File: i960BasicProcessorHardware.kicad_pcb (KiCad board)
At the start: 4 copper layers, 169.9 x 169.8 mm, 70 parts, among them J1 Conn_02x16_Odd_Even, J10 Conn_01x03, J11 Conn_01x08, J2 Conn_02x39_Odd_Even, J3 Conn_01x03, J4 Conn_02x05_Odd_Even, J5 Conn_02x05_Odd_Even, J6 Conn_02x05_Odd_Even, J7 Conn_01x06, J8 Conn_01x06, J9 Conn_01x11, SW1 SW_Push, U1 74HC245, U10 74LS08, U11 74LS04, U12 74LS174, U13 SN74LVC245AN, U14 74LS174, U15 MCP23S17_SP, U16 MCP23S17_SP, U17 MCP23S17_SP, U18 ATtiny85-20PU, U2 80960Sx, U3 MCP23S17_SP, U4 74HC245, U5 74HC573, U6 74HC573, U7 Adafruit_FeatherWing (PSRAM F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, U8 Adafruit_FeatherWing (PSRAM F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, U9 74LS125

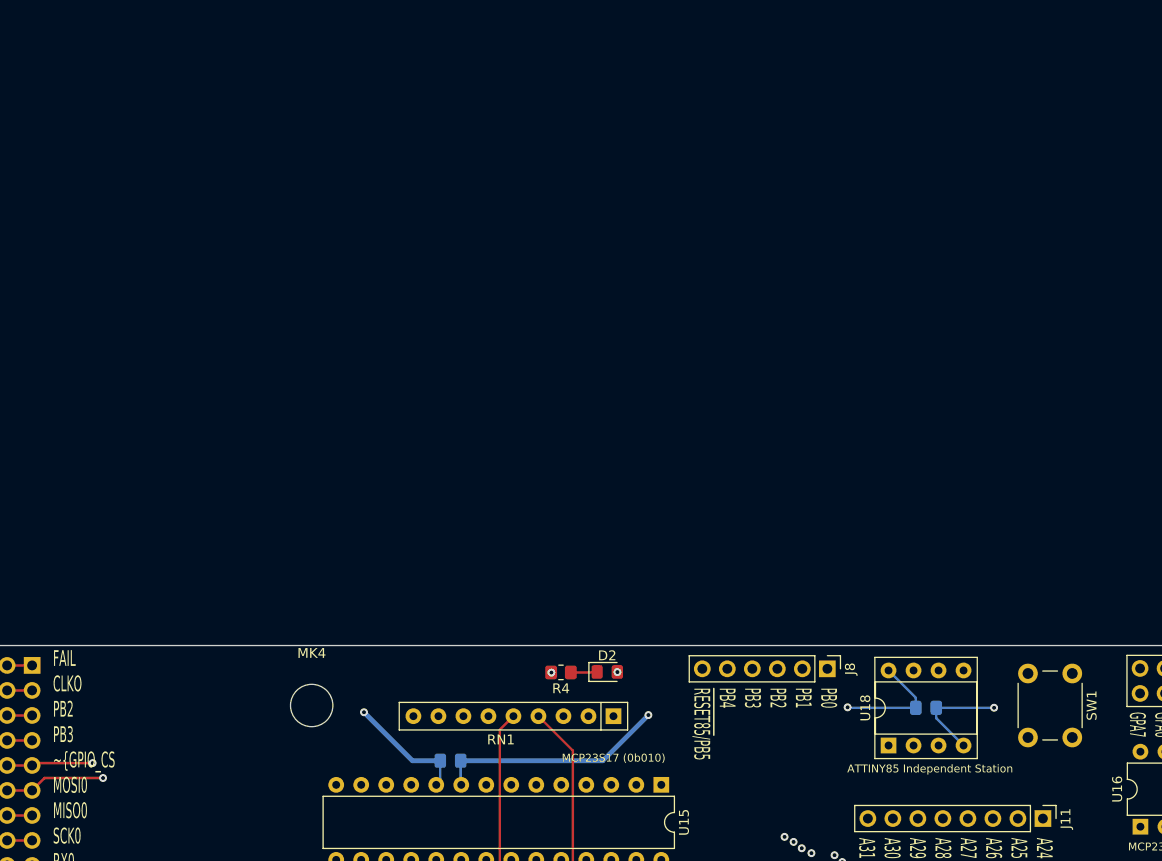
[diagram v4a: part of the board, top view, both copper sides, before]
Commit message: Drop the attiny85
I am going to place two 861s instead tied to the same 20mhz clock

I am also considering adding a dip40 socket also tied to the same
20mhz clock
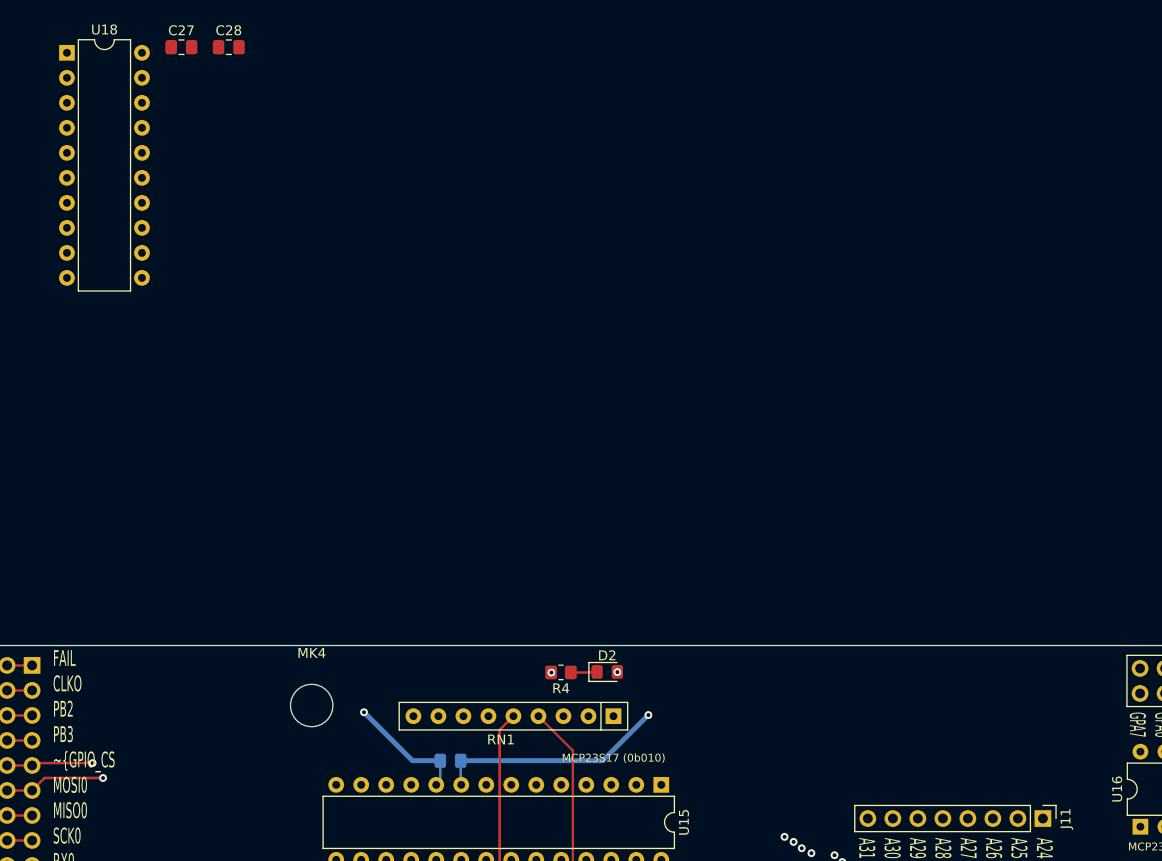
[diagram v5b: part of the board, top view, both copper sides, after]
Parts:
- removed J8: Conn_01x06, Connector_PinHeader_2.54mm:PinHeader_1x06_P2.54mm_Vertical
- removed SW1: SW_Push, Button_Switch_THT:SW_PUSH_6mm_H4.3mm
- added C28: 0.1uF, Capacitor_SMD:C_0805_2012Metric_Pad1.18x1.45mm_HandSolder, F.Cu at (41.5, -30.8)
- C27: moved to F.Cu
- U18: value ATtiny85-20PU -> ATtiny861-20PU; footprint Package_DIP:DIP-8_W7.62mm_Socket -> Package_DIP:DIP-20_W7.62mm
- moved U18 109.1 mm to (25.1, -30.2), turned to 0 degrees
- moved C27 101.1 mm to (36.7, -30.8)
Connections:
- U18 pad 1: /~RESET85 -> Net-(U18-Pad1)
- U18 pad 2: /ATTINY85_PB3 -> Net-(U18-Pad2)
- U18 pad 3: /ATTINY85_PB4 -> Net-(U18-Pad3)
- U18 pad 4: GND -> Net-(U18-Pad4)
- U18 pad 5: /ATTINY85_PB0 -> +5V
- U18 pad 6: /ATTINY85_PB1 -> GND
- U18 pad 7: /ATTINY85_PB2 -> /CLKO
- U18 pad 8: +5V -> GND
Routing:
- net /~RESET85: track 67.8 -> 0.00 mm
- net /ATTINY85_PB4: track 26.3 -> 0.00 mm
- net /ATTINY85_PB3: track 19.6 -> 0.00 mm
- net /ATTINY85_PB1: track 15.8 -> 0.00 mm
- net /ATTINY85_PB2: track 15.2 -> 0.00 mm
- net /ATTINY85_PB0: track 15.2 -> 0.00 mm
- net +5V: track 293.8 -> 281.9 mm, vias 26 -> 25
- net GND: track 405.7 -> 394.8 mm, vias 28 -> 27
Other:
- board text removed: "ATTINY85 Independent Station"
- board text removed: "PB0 PB1 PB2 PB3 PB4 ~RESET85~/PB5"

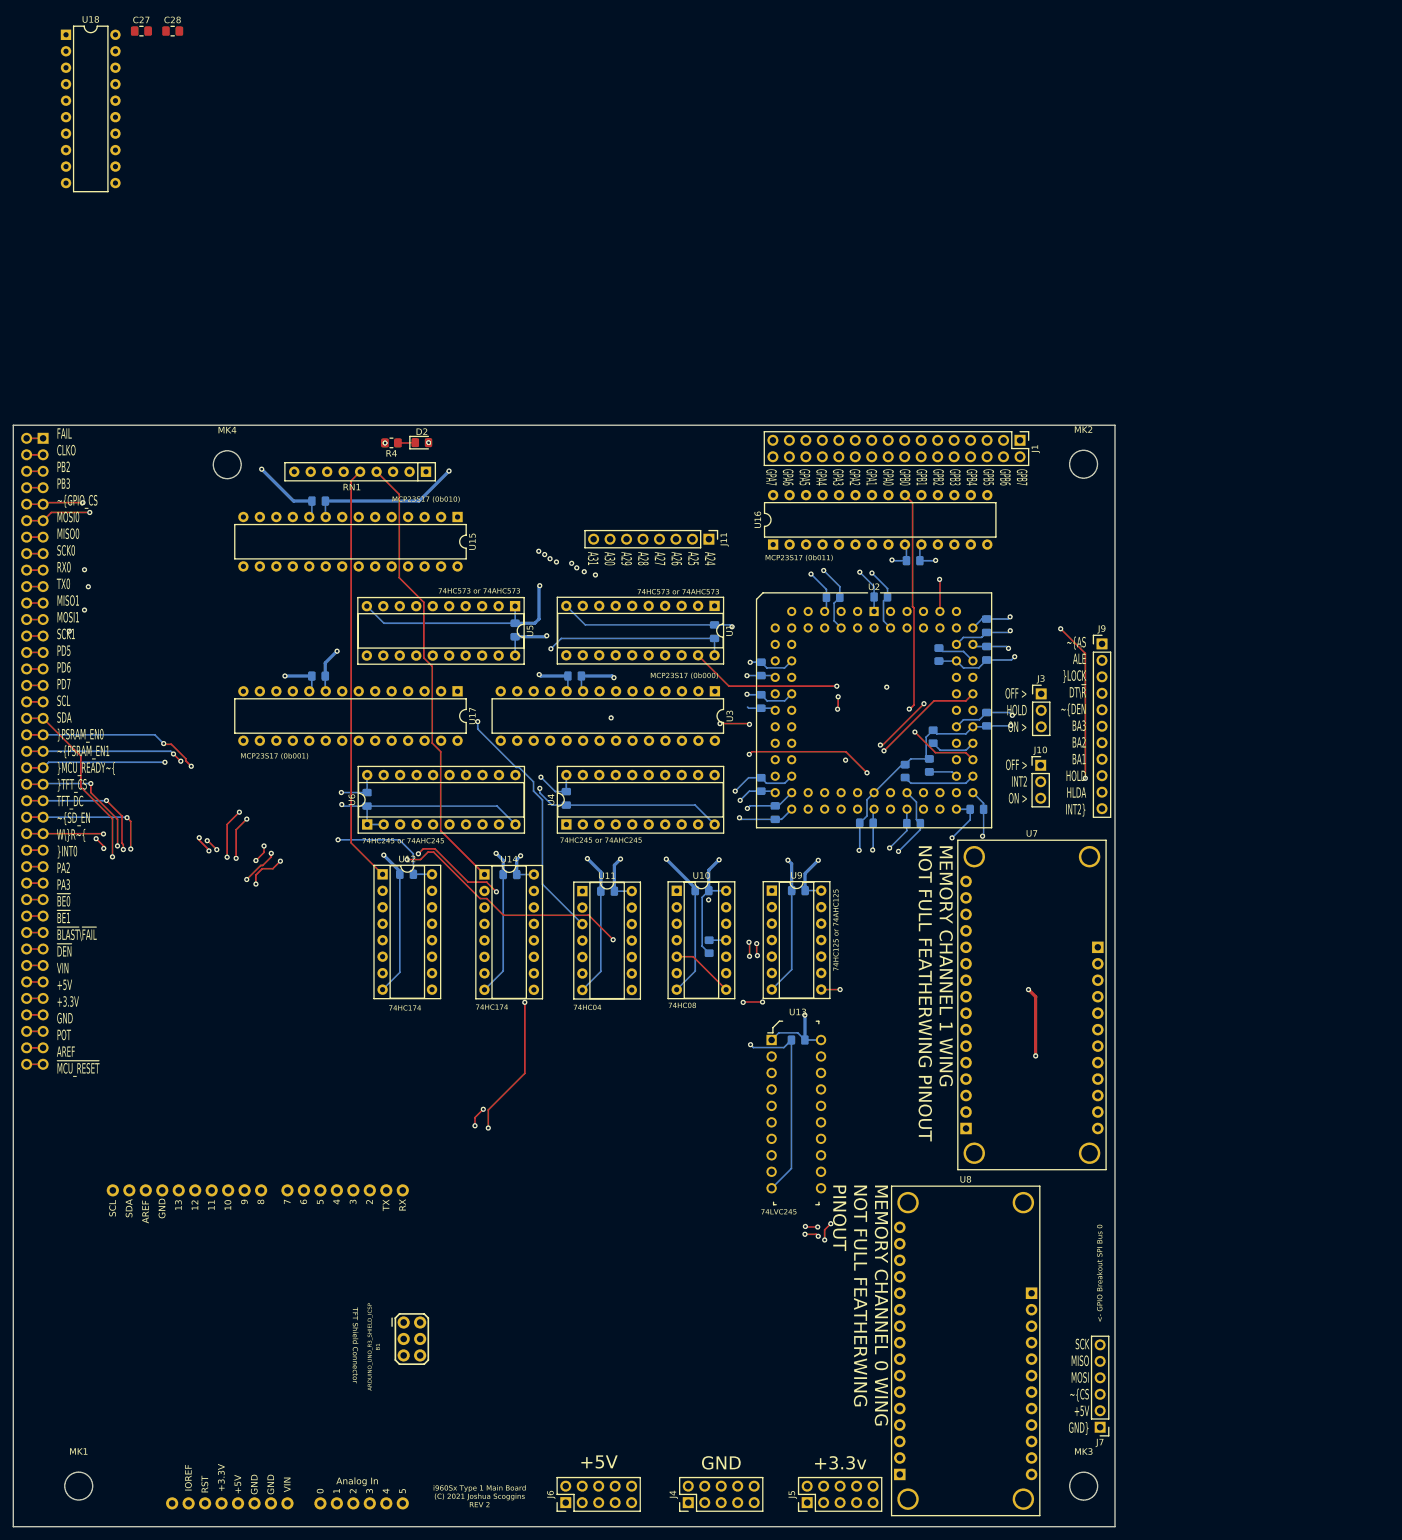
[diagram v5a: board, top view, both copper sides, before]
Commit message: We always have access to the 861s
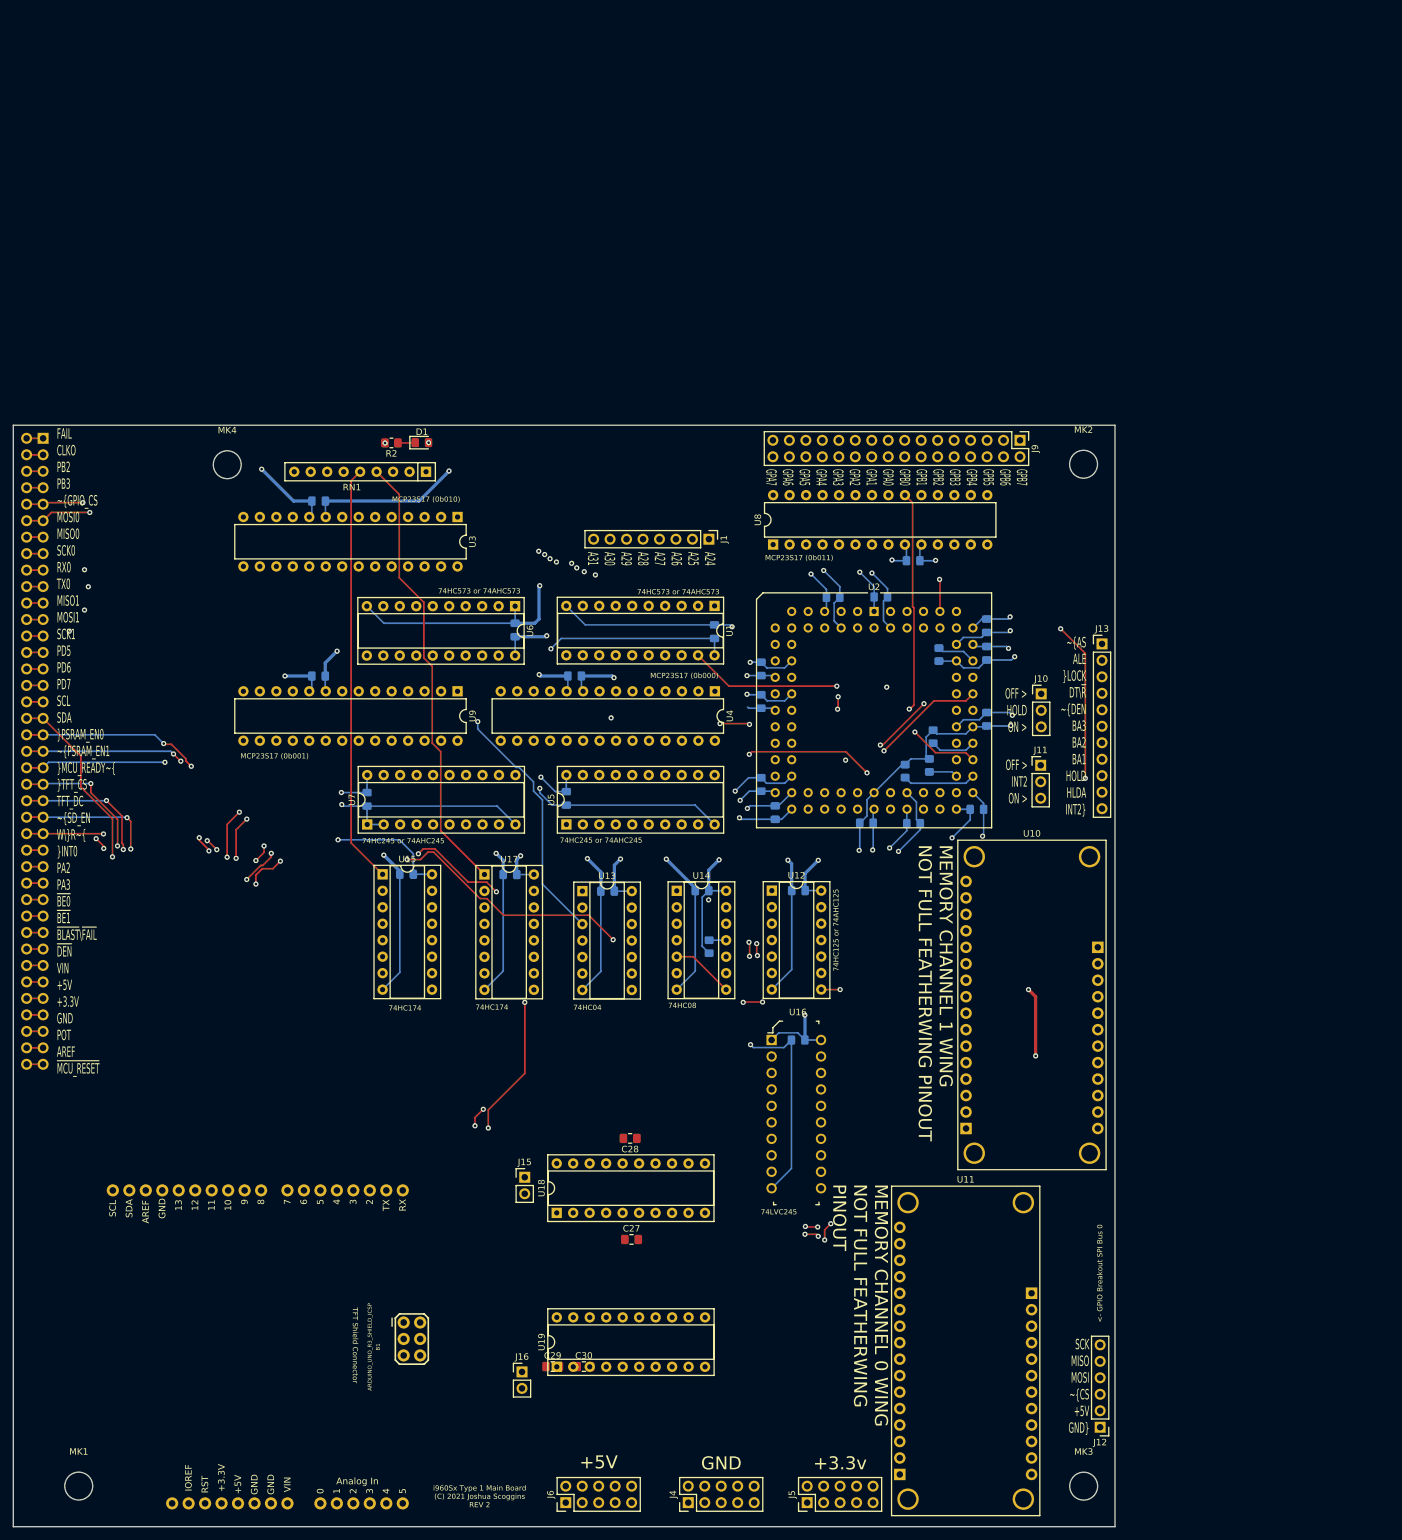
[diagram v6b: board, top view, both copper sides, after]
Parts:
- added C29: 0.1uF, Capacitor_SMD:C_0805_2012Metric_Pad1.18x1.45mm_HandSolder, F.Cu at (100.1, 175.1)
- added C30: 0.1uF, Capacitor_SMD:C_0805_2012Metric_Pad1.18x1.45mm_HandSolder, F.Cu at (105.0, 175.1)
- added J15: Conn_01x02, Connector_PinHeader_2.54mm:PinHeader_1x02_P2.54mm_Vertical, F.Cu at (95.8, 145.9)
- added J16: Conn_01x02, Connector_PinHeader_2.54mm:PinHeader_1x02_P2.54mm_Vertical, F.Cu at (95.4, 176.0)
- added U19: ATtiny861-20PU, Package_DIP:DIP-20_W7.62mm_Socket, F.Cu at (100.8, 175.2)
- U18: footprint Package_DIP:DIP-20_W7.62mm -> Package_DIP:DIP-20_W7.62mm_Socket
- moved C27 201.1 mm to (112.3, 155.5)
- moved U18 196.8 mm to (100.8, 151.4), turned to 90 degrees
- moved C28 184.7 mm to (112.1, 140.0), turned to 180 degrees
- renumbered C24 to C14, C14 to C15, C15 to C16, C16 to C17, C17 to C18, C25 to C19, C26 to C20, C18 to C21, C19 to C22, C20 to C23, C21 to C24, C22 to C25, C23 to C26, D2 to D1, J11 to J1, J3 to J10, J10 to J11, J7 to J12, J9 to J13, J2 to J14, J1 to J9, R4 to R2, R2 to R3, R3 to R4, U7 to U10, U8 to U11, U9 to U12, U11 to U13, U10 to U14, U12 to U15, U13 to U16, U14 to U17, U15 to U3, U3 to U4, U4 to U5, U5 to U6, U6 to U7, U16 to U8, U17 to U9
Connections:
- net /AVR861_INT0 renamed /Coprocessor0/PB6
- net /~RESET85 renamed Net-(RN1-Pad6)
- net Net-(U18-Pad1) renamed /Coprocessor0/PB0
- net Net-(U18-Pad11) renamed /Coprocessor0/PA7
- net Net-(U18-Pad12) renamed /Coprocessor0/PA6
- net Net-(U18-Pad13) renamed /Coprocessor0/PA5
- net Net-(U18-Pad14) renamed /Coprocessor0/PA4
- net Net-(U18-Pad17) renamed /Coprocessor0/PA3
- net Net-(U18-Pad18) renamed /Coprocessor0/PA2
- net Net-(U18-Pad19) renamed /Coprocessor0/PA1
- net Net-(U18-Pad2) renamed /Coprocessor0/PB1
- net Net-(U18-Pad20) renamed /Coprocessor0/PA0
- net Net-(U18-Pad3) renamed /Coprocessor0/PB2
- net Net-(U18-Pad4) renamed /Coprocessor0/PB3
- C27 pad 1: +5V -> VCC
- C28 pad 1: +5V -> VCC
- U18 pad 15: +5V -> VCC
- U18 pad 5: +5V -> VCC

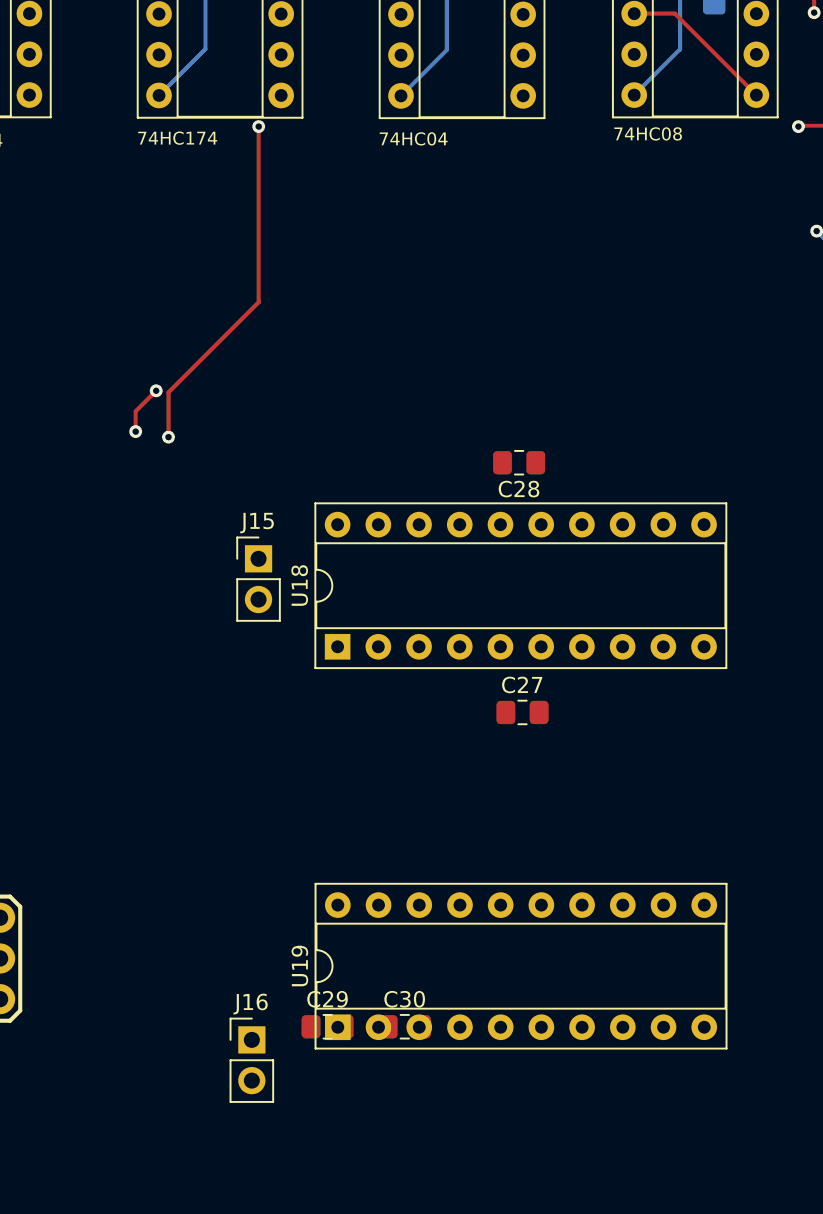
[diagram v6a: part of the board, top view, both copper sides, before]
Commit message: pull in a 1284p socket setup
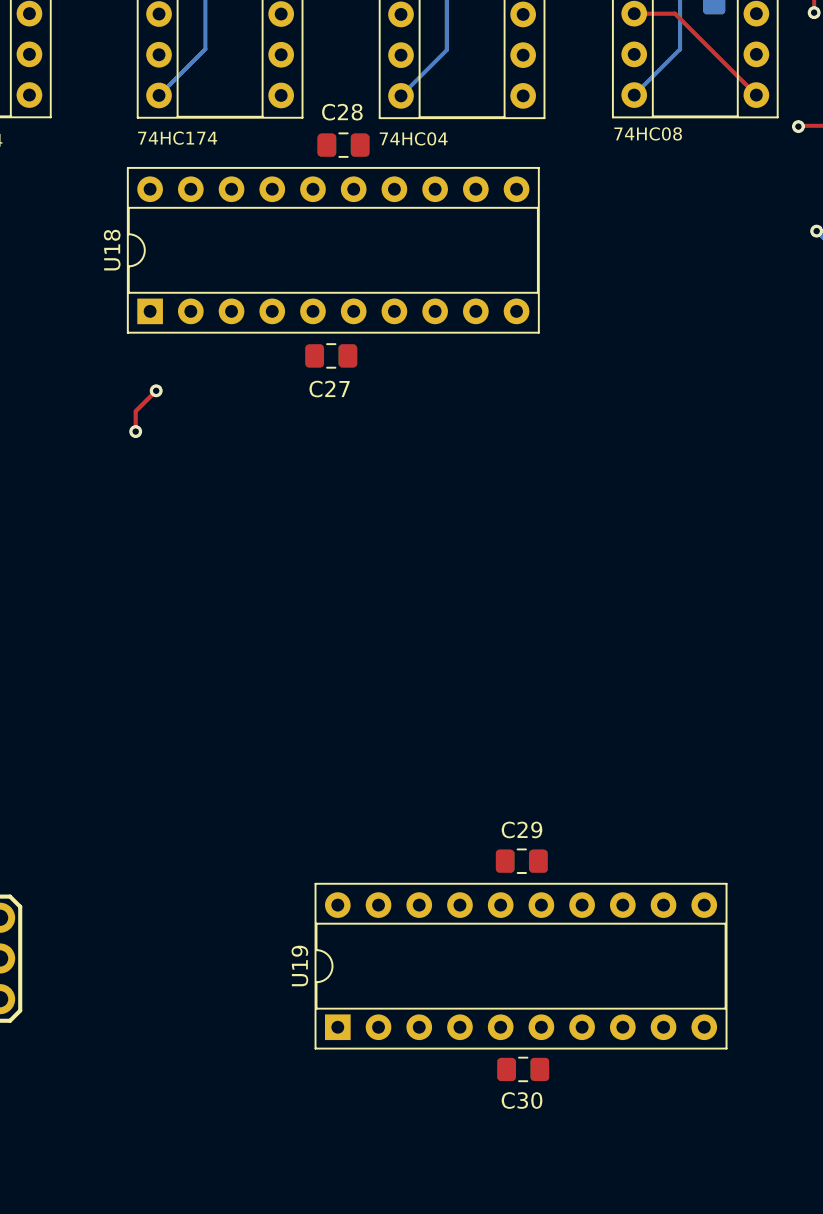
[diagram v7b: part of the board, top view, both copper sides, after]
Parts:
- removed J15, J16: Conn_01x02, Connector_PinHeader_2.54mm:PinHeader_1x02_P2.54mm_Vertical
- moved C27 25.2 mm to (100.4, 133.3)
- moved U18 24.0 mm to (89.1, 130.5)
- moved C28 22.6 mm to (101.1, 120.1)
- moved C29 15.9 mm to (112.3, 164.8), turned to 180 degrees
- moved C30 7.85 mm to (112.3, 177.8)
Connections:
- C27 pad 1: VCC -> +5V
- C28 pad 1: VCC -> +5V
- C29 pad 1: VCC -> +5V
- C30 pad 1: VCC -> +5V
- U18 pad 15: VCC -> +5V
- U18 pad 5: VCC -> +5V
- U19 pad 15: VCC -> +5V
- U19 pad 5: VCC -> +5V
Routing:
- net /MISO0: track 499.4 -> 442.0 mm, vias 9 -> 7
